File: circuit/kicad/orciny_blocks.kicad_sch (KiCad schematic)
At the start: 0 parts

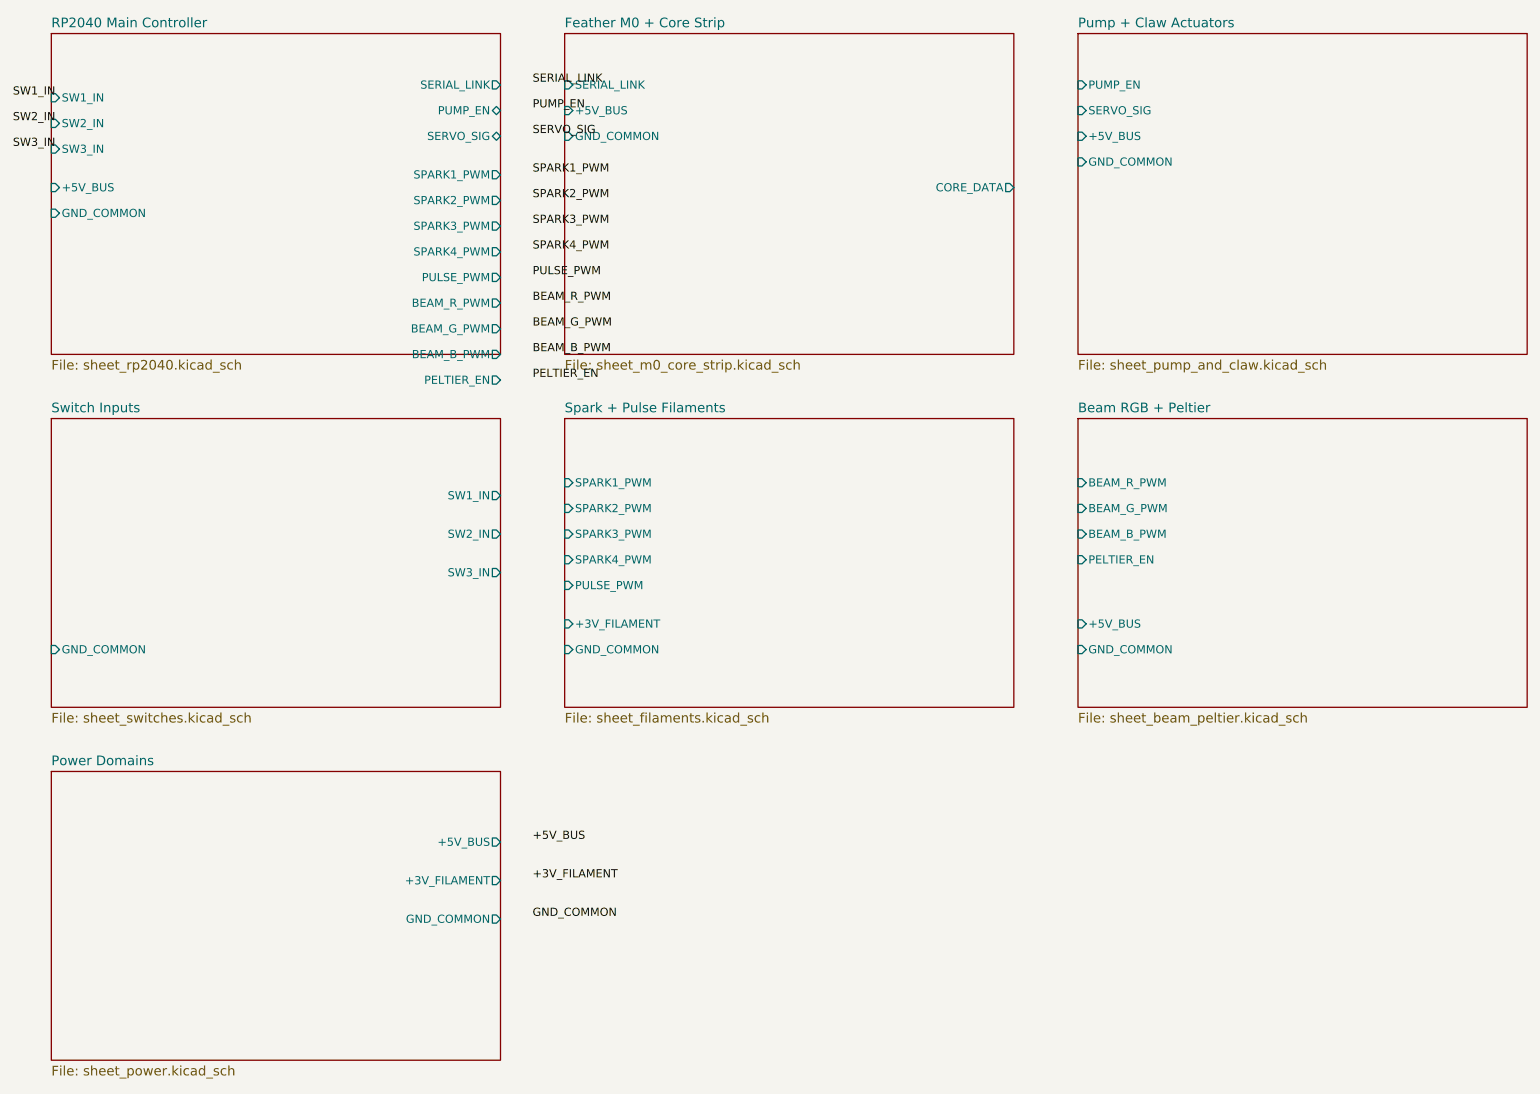
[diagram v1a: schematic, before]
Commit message: Sync KiCad schematics with current hardware
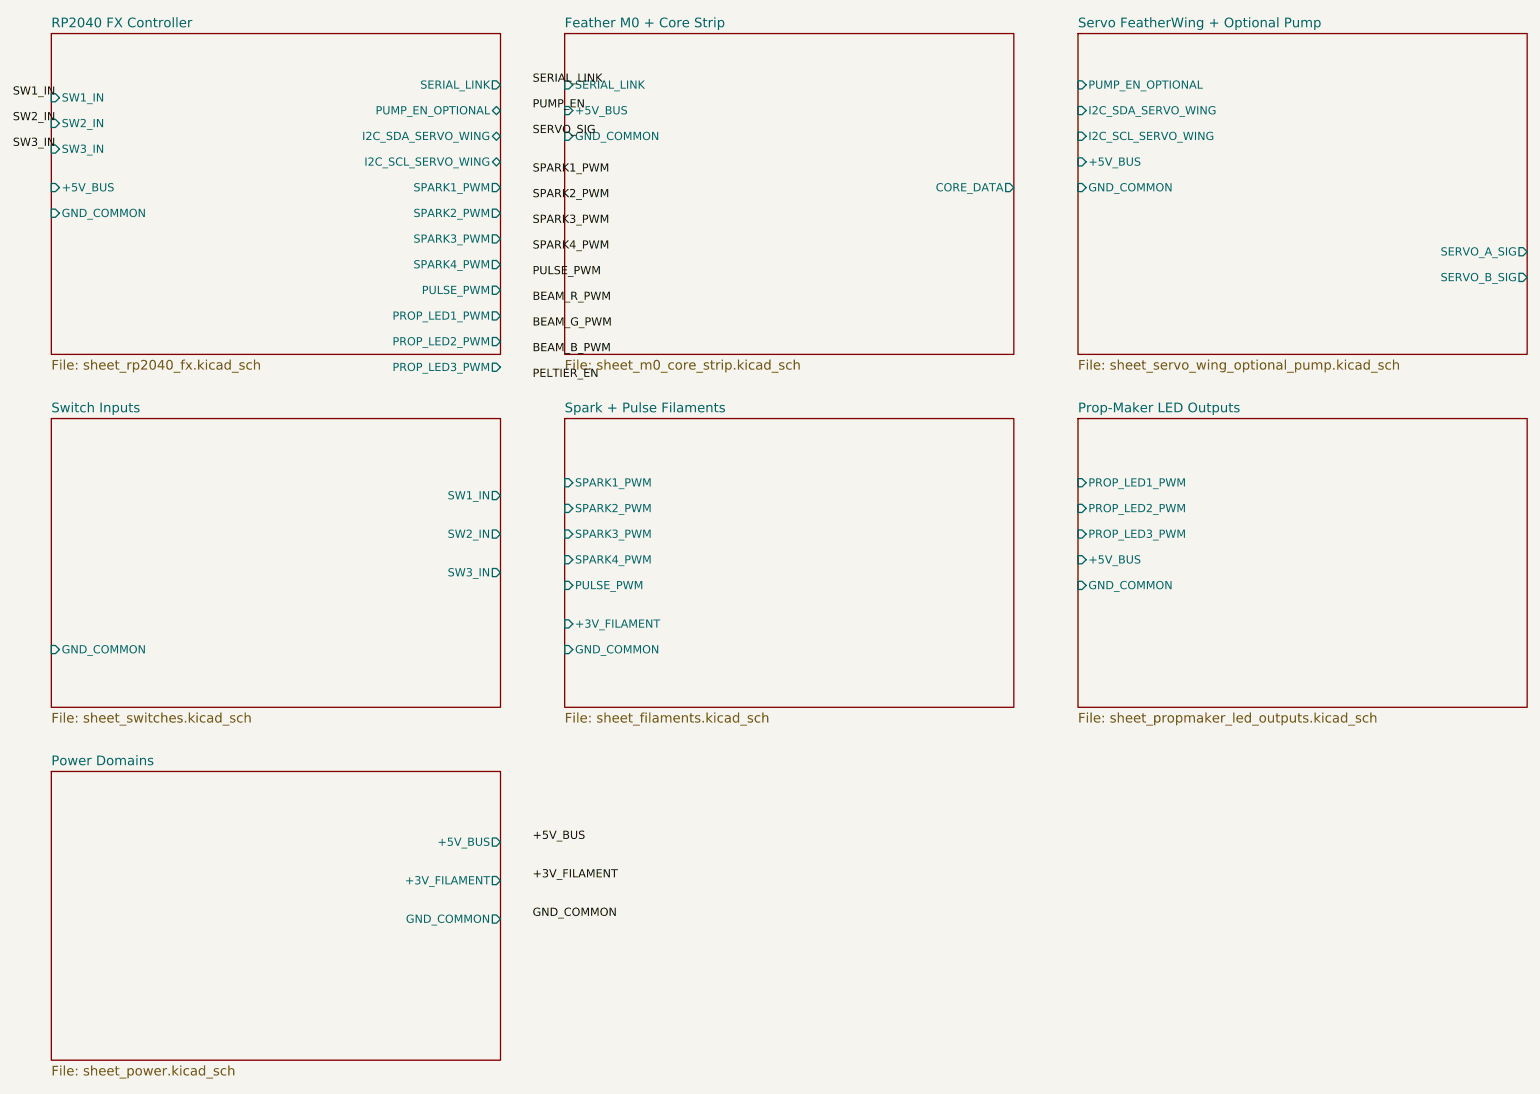
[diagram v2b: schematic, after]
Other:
- sheet Beam RGB + Peltier renamed Prop-Maker LED Outputs
- sheet Pump + Claw Actuators renamed Servo FeatherWing + Optional Pump
- sheet RP2040 Main Controller renamed RP2040 FX Controller
- sheet Prop-Maker LED Outputs: file sheet_beam_peltier.kicad_sch -> sheet_propmaker_led_outputs.kicad_sch
- sheet Prop-Maker LED Outputs ports: added PROP_LED1_PWM, PROP_LED2_PWM, PROP_LED3_PWM; removed BEAM_B_PWM, BEAM_G_PWM, BEAM_R_PWM, PELTIER_EN
- sheet RP2040 FX Controller: file sheet_rp2040.kicad_sch -> sheet_rp2040_fx.kicad_sch
- sheet RP2040 FX Controller ports: added I2C_SCL_SERVO_WING, I2C_SDA_SERVO_WING, PROP_LED1_PWM, PROP_LED2_PWM, PROP_LED3_PWM, PUMP_EN_OPTIONAL; removed BEAM_B_PWM, BEAM_G_PWM, BEAM_R_PWM, PELTIER_EN, PUMP_EN, SERVO_SIG
- sheet Servo FeatherWing + Optional Pump: file sheet_pump_and_claw.kicad_sch -> sheet_servo_wing_optional_pump.kicad_sch
- sheet Servo FeatherWing + Optional Pump ports: added I2C_SCL_SERVO_WING, I2C_SDA_SERVO_WING, PUMP_EN_OPTIONAL, SERVO_A_SIG, SERVO_B_SIG; removed PUMP_EN, SERVO_SIG
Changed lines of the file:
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@@
     (stroke (width 0) (type solid) (color 0 0 0 0))
     (fill (color 0 0 0 0.0000))
-    (property "Sheet name" "RP2040 Main Controller" (id 0) (at 20.00 19.20 0)
+    (property "Sheet name" "RP2040 FX Controller" (id 0) (at 20.00 19.20 0)
       (effects (font (size 1.50 1.50)) (justify left bottom))
     )
-    (property "Sheet file" "sheet_rp2040.kicad_sch" (id 1) (at 20.00 70.80 0)
+    (property "Sheet file" "sheet_rp2040_fx.kicad_sch" (id 1) (at 20.00 70.80 0)
       (effects (font (size 1.50 1.50)) (justify left top))
     )
@@
       (effects (font (size 1.27 1.27)) (justify right))
     )
-    (pin "PUMP_EN" bidirectional (at 90.00 32.00 0)
+    (pin "PUMP_EN_OPTIONAL" bidirectional (at 90.00 32.00 0)
       (effects (font (size 1.27 1.27)) (justify right))
     )
-    (pin "SERVO_SIG" bidirectional (at 90.00 36.00 0)
+    (pin "I2C_SDA_SERVO_WING" bidirectional (at 90.00 36.00 0)
       (effects (font (size 1.27 1.27)) (justify right))
     )
-    (pin "SPARK1_PWM" output (at 90.00 42.00 0)
+    (pin "I2C_SCL_SERVO_WING" bidirectional (at 90.00 40.00 0)
       (effects (font (size 1.27 1.27)) (justify right))
     )
-    (pin "SPARK2_PWM" output (at 90.00 46.00 0)
+    (pin "SPARK1_PWM" output (at 90.00 44.00 0)
       (effects (font (size 1.27 1.27)) (justify right))
     )
-    (pin "SPARK3_PWM" output (at 90.00 50.00 0)
+    (pin "SPARK2_PWM" output (at 90.00 48.00 0)
       (effects (font (size 1.27 1.27)) (justify right))
     )
-    (pin "SPARK4_PWM" output (at 90.00 54.00 0)
+    (pin "SPARK3_PWM" output (at 90.00 52.00 0)
       (effects (font (size 1.27 1.27)) (justify right))
     )
-    (pin "PULSE_PWM" output (at 90.00 58.00 0)
+    (pin "SPARK4_PWM" output (at 90.00 56.00 0)
       (effects (font (size 1.27 1.27)) (justify right))
     )
-    (pin "BEAM_R_PWM" output (at 90.00 62.00 0)
+    (pin "PULSE_PWM" output (at 90.00 60.00 0)
       (effects (font (size 1.27 1.27)) (justify right))
     )
-    (pin "BEAM_G_PWM" output (at 90.00 66.00 0)
+    (pin "PROP_LED1_PWM" output (at 90.00 64.00 0)
       (effects (font (size 1.27 1.27)) (justify right))
     )
-    (pin "BEAM_B_PWM" output (at 90.00 70.00 0)
+    (pin "PROP_LED2_PWM" output (at 90.00 68.00 0)
       (effects (font (size 1.27 1.27)) (justify right))
     )
-    (pin "PELTIER_EN" output (at 90.00 74.00 0)
+    (pin "PROP_LED3_PWM" output (at 90.00 72.00 0)
       (effects (font (size 1.27 1.27)) (justify right))
     )
@@
     (stroke (width 0) (type solid) (color 0 0 0 0))
     (fill (color 0 0 0 0.0000))
-    (property "Sheet name" "Pump + Claw Actuators" (id 0) (at 180.00 19.20 0)
+    (property "Sheet name" "Servo FeatherWing + Optional Pump" (id 0) (at 180.00 19.20 0)
       (effects (font (size 1.50 1.50)) (justify left bottom))
     )
-    (property "Sheet file" "sheet_pump_and_claw.kicad_sch" (id 1) (at 180.00 70.80 0)
+    (property "Sheet file" "sheet_servo_wing_optional_pump.kicad_sch" (id 1) (at 180.00 70.80 0)
       (effects (font (size 1.50 1.50)) (justify left top))
     )
-    (pin "PUMP_EN" input (at 180.00 28.00 180)
+    (pin "PUMP_EN_OPTIONAL" input (at 180.00 28.00 180)
       (effects (font (size 1.27 1.27)) (justify left))
     )
-    (pin "SERVO_SIG" input (at 180.00 32.00 180)
+    (pin "I2C_SDA_SERVO_WING" input (at 180.00 32.00 180)
       (effects (font (size 1.27 1.27)) (justify left))
     )
-    (pin "+5V_BUS" input (at 180.00 36.00 180)
+    (pin "I2C_SCL_SERVO_WING" input (at 180.00 36.00 180)
       (effects (font (size 1.27 1.27)) (justify left))
     )
-    (pin "GND_COMMON" input (at 180.00 40.00 180)
+    (pin "+5V_BUS" input (at 180.00 40.00 180)
       (effects (font (size 1.27 1.27)) (justify left))
+    )
+    (pin "GND_COMMON" input (at 180.00 44.00 180)
+      (effects (font (size 1.27 1.27)) (justify left))
+    )
+    (pin "SERVO_A_SIG" output (at 250.00 54.00 0)
+      (effects (font (size 1.27 1.27)) (justify right))
+    )
+    (pin "SERVO_B_SIG" output (at 250.00 58.00 0)
+      (effects (font (size 1.27 1.27)) (justify right))
     )
   )
@@
     (stroke (width 0) (type solid) (color 0 0 0 0))
     (fill (color 0 0 0 0.0000))
-    (property "Sheet name" "Beam RGB + Peltier" (id 0) (at 180.00 79.20 0)
+    (property "Sheet name" "Prop-Maker LED Outputs" (id 0) (at 180.00 79.20 0)
       (effects (font (size 1.50 1.50)) (justify left bottom))
     )
-    (property "Sheet file" "sheet_beam_peltier.kicad_sch" (id 1) (at 180.00 125.80 0)
+    (property "Sheet file" "sheet_propmaker_led_outputs.kicad_sch" (id 1) (at 180.00 125.80 0)
       (effects (font (size 1.50 1.50)) (justify left top))
     )
-    (pin "BEAM_R_PWM" input (at 180.00 90.00 180)
+    (pin "PROP_LED1_PWM" input (at 180.00 90.00 180)
       (effects (font (size 1.27 1.27)) (justify left))
     )
-    (pin "BEAM_G_PWM" input (at 180.00 94.00 180)
+    (pin "PROP_LED2_PWM" input (at 180.00 94.00 180)
       (effects (font (size 1.27 1.27)) (justify left))
     )
-    (pin "BEAM_B_PWM" input (at 180.00 98.00 180)
+    (pin "PROP_LED3_PWM" input (at 180.00 98.00 180)
       (effects (font (size 1.27 1.27)) (justify left))
     )
-    (pin "PELTIER_EN" input (at 180.00 102.00 180)
+    (pin "+5V_BUS" input (at 180.00 102.00 180)
       (effects (font (size 1.27 1.27)) (justify left))
     )
-    (pin "+5V_BUS" input (at 180.00 112.00 180)
+    (pin "GND_COMMON" input (at 180.00 106.00 180)
       (effects (font (size 1.27 1.27)) (justify left))
     )
-    (pin "GND_COMMON" input (at 180.00 116.00 180)
-      (effects (font (size 1.27 1.27)) (justify left))
-    )

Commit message: updated paperwork
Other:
- sheet Spark + Pulse Filaments renamed Spark Filaments
- sheet RP2040 FX Controller ports: added none; removed PULSE_PWM
- sheet Spark Filaments ports: added none; removed PULSE_PWM
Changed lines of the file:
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@@
-      (effects (font (size 1.27 1.27)) (justify right))
-    )
-    (pin "PULSE_PWM" output (at 90.00 60.00 0)
       (effects (font (size 1.27 1.27)) (justify right))
     )
@@
     (stroke (width 0) (type solid) (color 0 0 0 0))
     (fill (color 0 0 0 0.0000))
-    (property "Sheet name" "Spark + Pulse Filaments" (id 0) (at 100.00 79.20 0)
+    (property "Sheet name" "Spark Filaments" (id 0) (at 100.00 79.20 0)
       (effects (font (size 1.50 1.50)) (justify left bottom))
     )
@@
     )
     (pin "SPARK4_PWM" input (at 100.00 102.00 180)
-      (effects (font (size 1.27 1.27)) (justify left))
-    )
-    (pin "PULSE_PWM" input (at 100.00 106.00 180)
       (effects (font (size 1.27 1.27)) (justify left))
     )
@@
     (effects (font (size 1.27 1.27)) (justify left bottom))
   )
-  (label "PULSE_PWM" (at 95.00 58.00 0)
-    (effects (font (size 1.27 1.27)) (justify left bottom))
-  )
